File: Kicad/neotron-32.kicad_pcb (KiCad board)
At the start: 4 copper layers, 166.9 x 140.7 mm, 97 parts, among them J1001 Conn_02x05, J101 Conn_02x06, J102 Conn_02x06, J103 Conn_02x04, J201 DIN-5 180 degree, J202 DIN-5 180 degree, J301 3.5mm Audio Jack TRS, J302 Conn_01x03_Male, J401 USB_B, J501 micro SD Card, J601 Conn_02x13_Header, J701 AVR-ISP-6, J702 DE9 Male, J703 DE9 Male, J704 Double-mini-DIN-6, J901 DB15HD_Female, SW401 SW_Push_DPDT_ON_OFF, SW402 SW_Push_DPDT_ON_MO, U1001 ICL3232CPZMAX, U101 EK-TM4C123GXL, U201 74LS14, U202 6N138, U401 TC1262-33, U601 MCP23S17_SP, U701 ATmega328-PU, U801 MCP7940N-xP, Y801 32,768 Hz

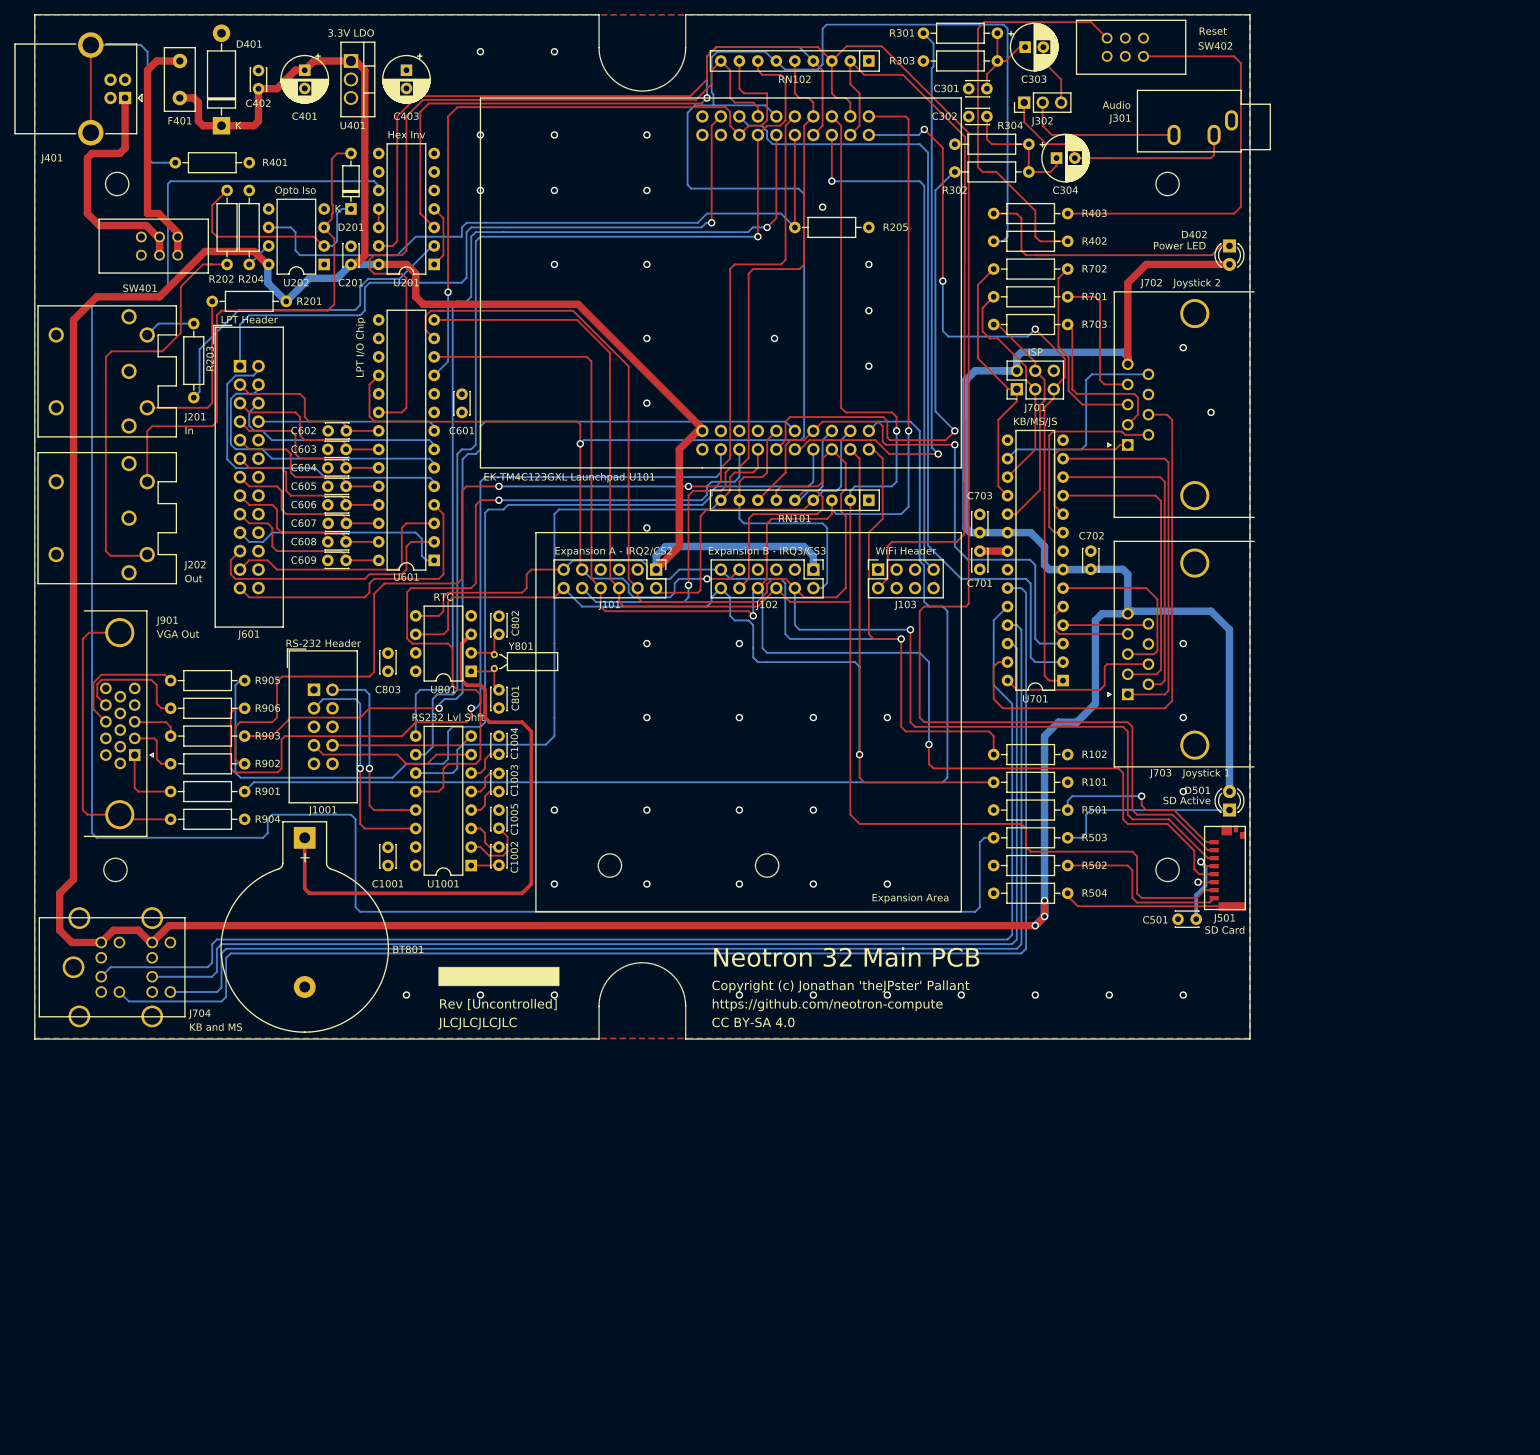
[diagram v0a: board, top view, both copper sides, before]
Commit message: Switch to 1598D enclosure.
Use MIC2005A current limiter on input.
Use soft on/off switch from Atmega.
Atmega connects to Tiva over I2C.
Use full-size SD card.
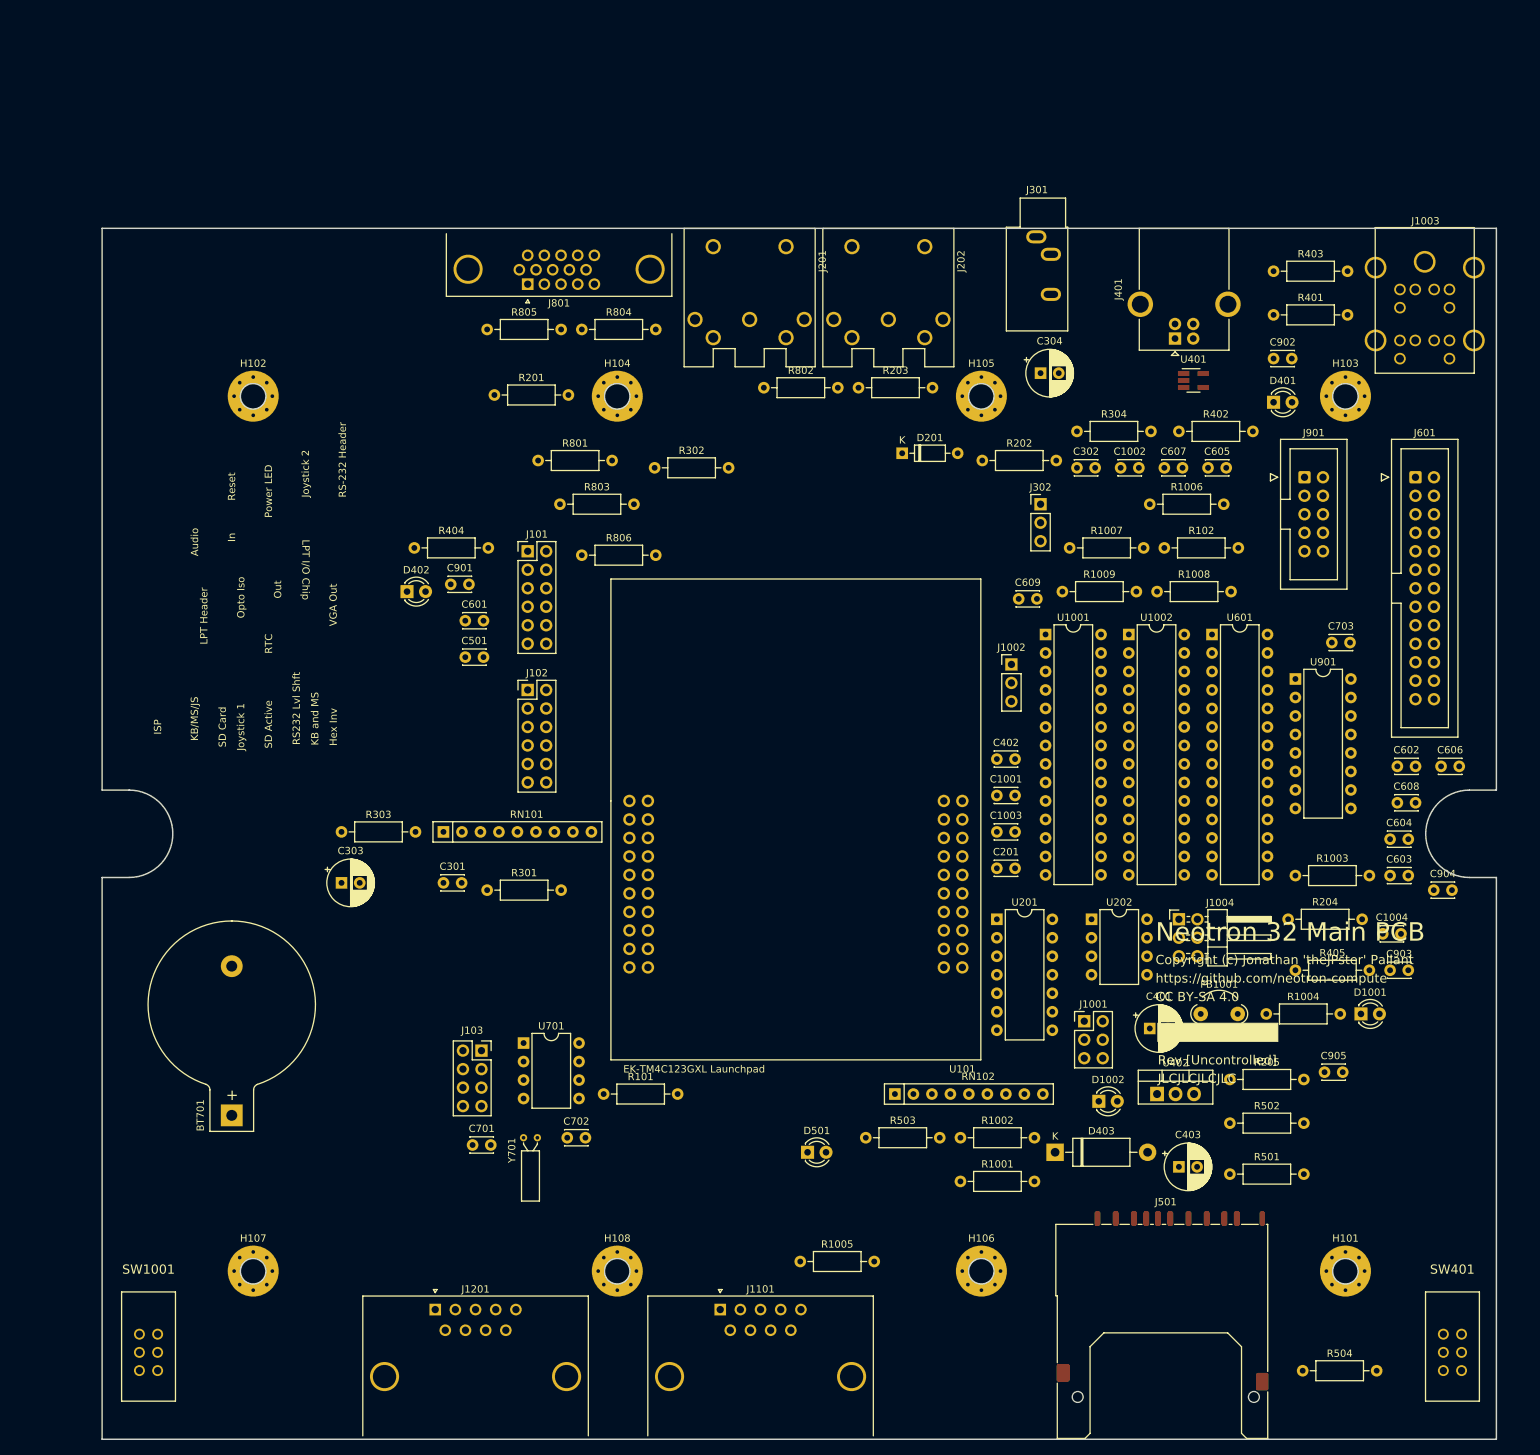
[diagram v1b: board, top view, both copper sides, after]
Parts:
- removed BT801: CR2032, Neotron 32:BatteryHolder_Keystone_103_1x20mm
- removed C1005, C803: 100n, Capacitor_THT:C_Disc_D3.0mm_W2.0mm_P2.50mm
- removed C801, C802: 6p, Capacitor_THT:C_Disc_D3.0mm_W2.0mm_P2.50mm
- removed F401: 250mA PTC, Fuse:Fuse_Littelfuse_395Series
- removed J701: AVR-ISP-6, Connector_PinHeader_2.54mm:PinHeader_2x03_P2.54mm_Vertical
- removed J702, J703: DE9 Male, Connector_Dsub:DSUB-9_Male_Horizontal_P2.77x2.84mm_EdgePinOffset14.56mm_Housed_MountingHolesOffset8.20mm
- removed J704: Double-mini-DIN-6, Neotron 32:Double_mini-DIN_6
- removed R701, R702, R703: 1k, Resistor_THT:R_Axial_DIN0207_L6.3mm_D2.5mm_P10.16mm_Horizontal
- removed R901, R902, R903, R905, R906: 330, Resistor_THT:R_Axial_DIN0207_L6.3mm_D2.5mm_P10.16mm_Horizontal
- removed R904: DNF, Resistor_THT:R_Axial_DIN0207_L6.3mm_D2.5mm_P10.16mm_Horizontal
- removed SW402: SW_Push_DPDT_ON_MO, Neotron 32:PHB2UEETS1A
- removed U801: MCP7940N-xP, Package_DIP:DIP-8_W7.62mm
- removed Y801: 32,768 Hz, Crystal:Crystal_C26-LF_D2.1mm_L6.5mm_Horizontal
- added BT701: CR2032, Neotron 32:BatteryHolder_Keystone_103_1x20mm, F.Cu at (97.9, 168.9)
- added C901: 100n, Capacitor_THT:C_Disc_D3.0mm_W2.0mm_P2.50mm, F.Cu at (128.0, 96.0)
- added C902: 100n, Capacitor_THT:C_Disc_D3.0mm_W2.0mm_P2.50mm, F.Cu at (241.0, 65.0)
- added C903: 100n, Capacitor_THT:C_Disc_D3.0mm_W2.0mm_P2.50mm, F.Cu at (257.0, 149.0)
- added C904: 100n, Capacitor_THT:C_Disc_D3.0mm_W2.0mm_P2.50mm, F.Cu at (263.0, 138.0)
- added C905: 100n, Capacitor_THT:C_Disc_D3.0mm_W2.0mm_P2.50mm, F.Cu at (248.0, 163.0)
- added D1001: LED, LED_THT:LED_D3.0mm, F.Cu at (253.0, 155.0)
- added D1002: LED, LED_THT:LED_D3.0mm, F.Cu at (217.0, 167.0)
- added D403: SA5.0A, Diode_THT:D_DO-15_P12.70mm_Horizontal, F.Cu at (211.0, 174.0)
- added FB1001: 100R, Ferrite_THT:LairdTech_28C0236-0JW-10, F.Cu at (231.0, 155.0)
- added H107: MountingHole, MountingHole:MountingHole_3.5mm_Pad_Via, F.Cu at (100.9, 190.3)
- added H108: MountingHole, MountingHole:MountingHole_3.5mm_Pad_Via, F.Cu at (150.9, 190.3)
- added J1002: 1x3 UART Debug Header, Connector_PinHeader_2.54mm:PinHeader_1x03_P2.54mm_Vertical, F.Cu at (205.0, 107.0)
- added J1003: Double-mini-DIN-6, Neotron 32:Double_mini-DIN_6, F.Cu at (261.8, 47.0)
- added J1004: AVR-ISP-6, Connector_PinHeader_2.54mm:PinHeader_2x03_P2.54mm_Horizontal, F.Cu at (228.0, 142.0)
- added J1101: DE9 Male, Connector_Dsub:DSUB-9_Male_Horizontal_P2.77x2.84mm_EdgePinOffset14.56mm_Housed_MountingHolesOffset8.20mm, F.Cu at (165.0, 195.6)
- added J1201: DE9 Male, Connector_Dsub:DSUB-9_Male_Horizontal_P2.77x2.84mm_EdgePinOffset14.56mm_Housed_MountingHolesOffset8.20mm, F.Cu at (125.9, 195.6)
- added J801: DB15HD_Female, Connector_Dsub:DSUB-15-HD_Female_Horizontal_P2.29x1.98mm_EdgePinOffset3.03mm_Housed_MountingHolesOffset4.94mm, F.Cu at (138.6, 54.8)
- added R1001: 10k, Resistor_THT:R_Axial_DIN0207_L6.3mm_D2.5mm_P10.16mm_Horizontal, F.Cu at (198.0, 178.0)
- added R1002: 10k, Resistor_THT:R_Axial_DIN0207_L6.3mm_D2.5mm_P10.16mm_Horizontal, F.Cu at (198.0, 172.0)
- added R1003: 10k, Resistor_THT:R_Axial_DIN0207_L6.3mm_D2.5mm_P10.16mm_Horizontal, F.Cu at (244.0, 136.0)
- added R1004: 1k, Resistor_THT:R_Axial_DIN0207_L6.3mm_D2.5mm_P10.16mm_Horizontal, F.Cu at (240.0, 155.0)
- added R1005: 1k, Resistor_THT:R_Axial_DIN0207_L6.3mm_D2.5mm_P10.16mm_Horizontal, F.Cu at (176.0, 189.0)
- added R1006: 6.81k 1%, Resistor_THT:R_Axial_DIN0207_L6.3mm_D2.5mm_P10.16mm_Horizontal, F.Cu at (224.0, 85.0)
- added R1007: 1k 1%, Resistor_THT:R_Axial_DIN0207_L6.3mm_D2.5mm_P10.16mm_Horizontal, F.Cu at (213.0, 91.0)
- added R1008: 6.81k 1%, Resistor_THT:R_Axial_DIN0207_L6.3mm_D2.5mm_P10.16mm_Horizontal, F.Cu at (225.0, 97.0)
- added R1009: 1k 1%, Resistor_THT:R_Axial_DIN0207_L6.3mm_D2.5mm_P10.16mm_Horizontal, F.Cu at (212.0, 97.0)
- added R404: 1k, Resistor_THT:R_Axial_DIN0207_L6.3mm_D2.5mm_P10.16mm_Horizontal, F.Cu at (123.0, 91.0)
- added R405: 330, Resistor_THT:R_Axial_DIN0207_L6.3mm_D2.5mm_P10.16mm_Horizontal, F.Cu at (244.0, 149.0)
- added R801: 330, Resistor_THT:R_Axial_DIN0207_L6.3mm_D2.5mm_P10.16mm_Horizontal, F.Cu at (140.0, 79.0)
- added R802: 330, Resistor_THT:R_Axial_DIN0207_L6.3mm_D2.5mm_P10.16mm_Horizontal, F.Cu at (171.0, 69.0)
- added R803: 330, Resistor_THT:R_Axial_DIN0207_L6.3mm_D2.5mm_P10.16mm_Horizontal, F.Cu at (143.0, 85.0)
- added R804: DNF, Resistor_THT:R_Axial_DIN0207_L6.3mm_D2.5mm_P10.16mm_Horizontal, F.Cu at (146.0, 61.0)
- added R805: 330, Resistor_THT:R_Axial_DIN0207_L6.3mm_D2.5mm_P10.16mm_Horizontal, F.Cu at (133.0, 61.0)
- added R806: 330, Resistor_THT:R_Axial_DIN0207_L6.3mm_D2.5mm_P10.16mm_Horizontal, F.Cu at (146.0, 92.0)
- added SW1001: SW_Push, Neotron 32:PHB2UEETS1A, F.Cu at (86.5, 200.7)
- added U1002: ATmega328P-PU, Package_DIP:DIP-28_W7.62mm, F.Cu at (221.1, 102.9)
- added U402: TC1262-33, Package_TO_SOT_THT:TO-220-3_Vertical, F.Cu at (225.0, 166.0)
- added U901: ICL3232CPZMAX, Package_DIP:DIP-16_W7.62mm, F.Cu at (244.0, 109.0)
- added Y701: 32,768 Hz, Crystal:Crystal_C26-LF_D2.1mm_L6.5mm_Horizontal, F.Cu at (138.0, 172.0)
- C701, C702: value 100n -> 6p
- D401: value SA5.0A -> LED; footprint Diode_THT:D_DO-15_P12.70mm_Horizontal -> LED_THT:LED_D3.0mm
- D402: value Red LED -> LED
- H101, H102, H103, H104, H105, H106: footprint MountingHole:MountingHole_3.2mm_M3 -> MountingHole:MountingHole_3.5mm_Pad_Via
- J1001: value Conn_02x05 -> 2x3 Header; footprint Connector_IDC:IDC-Header_2x05_P2.54mm_Vertical -> Connector_PinHeader_2.54mm:PinHeader_2x03_P2.54mm_Vertical
- J501: value micro SD Card -> SD_Card; footprint Neotron 32:Molex_4730_2651 -> Connector_Card:SD_Kyocera_145638109511859+
- J901: value DB15HD_Female -> Conn_02x05; footprint Connector_Dsub:DSUB-15-HD_Female_Horizontal_P2.29x1.98mm_EdgePinOffset3.03mm_Housed_MountingHolesOffset4.94mm -> Connector_IDC:IDC-Header_2x05_P2.54mm_Vertical
- R402: value 330 -> 100k
- R403: value 330 -> 1k
- SW401: value SW_Push_DPDT_ON_OFF -> SW_Push_DPDT_ON_MO
- U1001: value ICL3232CPZMAX -> MCP23017_SP; footprint Package_DIP:DIP-16_W7.62mm -> Package_DIP:DIP-28_W7.62mm
- U401: value TC1262-33 -> MIC2005A-2YM5; footprint Package_TO_SOT_THT:TO-220-3_Vertical -> Package_TO_SOT_SMD:SOT-23-5_HandSoldering
- U701: value ATmega328-PU -> MCP7940N-xP; footprint Package_DIP:DIP-28_W7.62mm -> Package_DIP:DIP-8_W7.62mm
- moved SW401 233.8 mm to (265.6, 200.7), turned to 270 degrees
- moved C403 184.2 mm to (228.0, 176.0), turned to 0 degrees
- moved H103 181.0 mm to (250.9, 70.2)
- moved C401 175.5 mm to (224.0, 157.0), turned to 0 degrees
- moved R204 174.3 mm to (243.0, 142.0), turned to 0 degrees
- moved J901 165.1 mm to (245.2, 81.3), turned to 0 degrees
- moved J601 162.1 mm to (260.5, 81.3)
- moved C603 157.2 mm to (257.0, 136.0)
- moved C606 157.0 mm to (264.0, 121.0)
- moved C604 154.5 mm to (257.0, 131.0)
- moved C602 153.9 mm to (258.0, 121.0)
- moved C608 151.2 mm to (258.0, 126.0)
- moved D401 149.4 mm to (241.0, 71.0), turned to 0 degrees
- moved C303 148.3 mm to (113.0, 137.0)
- moved J401 147.9 mm to (227.5, 62.2), turned to 90 degrees
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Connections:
- net /Power/UNFUSED_5V renamed Net-(R405-Pad2)
- C1001 pad 1: GND -> +5V
- C1001 pad 2: +3V3 -> GND
- C1002 pad 1: Net-(C1002-Pad1) -> GND
- C1003 pad 1: Net-(C1003-Pad1) -> +5V
- C1003 pad 2: Net-(C1003-Pad2) -> GND
- C1004 pad 1: GND -> Net-(C1004-Pad1)
- C1004 pad 2: Net-(C1004-Pad2) -> GND
- C702 pad 1: +5V -> Net-(C702-Pad1)
- C703 pad 1: +5V -> +3V3
- D401 pad 1: +5V -> Net-(D401-Pad1)
- D401 pad 2: GND -> Net-(D401-Pad2)
- D402 pad 1: Net-(D402-Pad1) -> GND
- D402 pad 2: +5V -> Net-(D402-Pad2)
- J1001 pad 1: Net-(J1001-Pad1) -> +5V
- J1001 pad 2: /RS-232 Serial Port/RS232_RX_IN -> Net-(J1001-Pad2)
- J1001 pad 3: /RS-232 Serial Port/RS232_TX_OUT -> +5V
- J1001 pad 5: GND -> +5V
- J103 pad 3: Net-(J103-Pad3) -> (no net)
- J103 pad 4: Net-(J103-Pad4) -> (no net)
- J103 pad 5: Net-(J103-Pad5) -> (no net)
- J103 pad 6: Net-(J103-Pad6) -> (no net)
- J201 pad 1: Net-(J201-Pad1) -> (no net)
- J201 pad 3: Net-(J201-Pad3) -> (no net)
- J202 pad 1: Net-(J202-Pad1) -> (no net)
- J202 pad 2: Net-(J202-Pad2) -> (no net)
- J202 pad 3: Net-(J202-Pad3) -> (no net)
- J401 pad 1: /Power/VUSB -> Net-(D401-Pad2)
- J401 pad 2: Net-(J401-Pad2) -> (no net)
- J401 pad 3: Net-(J401-Pad3) -> (no net)
- J501 pad 1: Net-(J501-Pad1) -> /~PA3_SPI_CS0
- J501 pad 12: (no net) -> Net-(J501-Pad12)
- J501 pad 2: /~PA3_SPI_CS0 -> /PA5_SPI_MOSI
- J501 pad 3: /PA5_SPI_MOSI -> GND
- J901 pad 1: Net-(J901-Pad1) -> (no net)
- J901 pad 10: Net-(J901-Pad10) -> (no net)
- J901 pad 2: Net-(J901-Pad2) -> /RS-232 Serial Port/RS232_RX_IN
- J901 pad 3: Net-(J901-Pad3) -> /RS-232 Serial Port/RS232_TX_OUT
- J901 pad 4: Net-(J901-Pad4) -> (no net)
- J901 pad 6: GND -> (no net)
- J901 pad 7: GND -> /RS-232 Serial Port/RS232_RTS_OUT
- J901 pad 8: GND -> /RS-232 Serial Port/RS232_CTS_IN
- J901 pad 9: Net-(J901-Pad9) -> (no net)
- R402 pad 1: /~RESET -> /~POWER_ON
- R402 pad 2: Net-(R402-Pad2) -> Net-(D401-Pad2)
- R403 pad 1: Net-(D402-Pad1) -> Net-(R403-Pad1)
- R403 pad 2: Net-(R403-Pad2) -> Net-(D401-Pad1)
- R501 pad 1: Net-(J501-Pad1) -> Net-(J501-Pad9)
- R504 pad 1: Net-(J501-Pad9) -> Net-(J501-Pad12)
- RN101 pad 7: /PE1_U7TX -> (no net)
- SW401 pad 1: Net-(SW401-Pad1) -> (no net)
- SW401 pad 2: /Power/VUSB -> GND
- SW401 pad 4: Net-(SW401-Pad4) -> (no net)
- SW401 pad 5: /Power/VUSB -> GND
- U1001 pad 1: Net-(C1002-Pad2) -> /Keyboard, Mouse and Joystick/JS1_UP
- U1001 pad 10: /PC4_U1RTS -> GND
- U1001 pad 11: /PB1_U1TX -> (no net)
- U1001 pad 12: /PB0_U1RX -> /PA6_I2C_SCL
- U1001 pad 13: /RS-232 Serial Port/RS232_RX_IN -> /PA7_I2C_SDA
- U1001 pad 14: /RS-232 Serial Port/RS232_TX_OUT -> (no net)
- U1001 pad 15: GND -> Net-(J1001-Pad6)
- U1001 pad 16: +3V3 -> Net-(J1001-Pad4)
- U1001 pad 2: Net-(C1005-Pad2) -> /Keyboard, Mouse and Joystick/JS1_DOWN
- U1001 pad 3: Net-(C1002-Pad1) -> /Keyboard, Mouse and Joystick/JS1_LEFT
- U1001 pad 4: Net-(C1003-Pad1) -> /Keyboard, Mouse and Joystick/JS1_RIGHT
- U1001 pad 5: Net-(C1003-Pad2) -> /Keyboard, Mouse and Joystick/JS1_A_B
- U1001 pad 6: Net-(C1004-Pad2) -> /Keyboard, Mouse and Joystick/JS1_START_C
- U1001 pad 7: /RS-232 Serial Port/RS232_RTS_OUT -> /Keyboard, Mouse and Joystick/JS1_SELECT
- U1001 pad 8: /RS-232 Serial Port/RS232_CTS_IN -> (no net)
- U1001 pad 9: /PC5_U1CTS -> +5V
- U101 pad 1.1: +3.3VP -> (no net)
- U101 pad 2.3: /PE0_U7RX -> (no net)
- U101 pad 3.3: Net-(U101-Pad3.3) -> (no net)
- U101 pad 3.4: Net-(U101-Pad3.4) -> (no net)
- U101 pad 3.7: /PE1_U7TX -> (no net)
- U101 pad 4.1: Net-(U101-Pad4.1) -> (no net)
- U101 pad 4.10: /~PF4_AT_RESET -> /~PF4_HID_IRQ
- U101 pad 4.2: Net-(U101-Pad4.2) -> (no net)
- U201 pad 6: Net-(U201-Pad6) -> (no net)
- U201 pad 8: Net-(U201-Pad8) -> (no net)
- U202 pad 1: Net-(U202-Pad1) -> (no net)
- U202 pad 4: Net-(U202-Pad4) -> (no net)
- U401 pad 1: +5V -> Net-(D401-Pad2)
- U401 pad 3: +3V3 -> /~POWER_ON
- U601 pad 19: Net-(U601-Pad19) -> (no net)
- U701 pad 1: /~PF4_AT_RESET -> Net-(C701-Pad2)
- U701 pad 2: /PE0_U7RX -> Net-(C702-Pad1)
- U701 pad 3: /PE1_U7TX -> +BATT
- U701 pad 4: /Keyboard, Mouse and Joystick/START_C_JS1 -> GND
- U701 pad 5: /Keyboard, Mouse and Joystick/RIGHT_GND_JS1 -> /PA7_I2C_SDA
- U701 pad 6: /Keyboard, Mouse and Joystick/LEFT_GND_JS1 -> /PA6_I2C_SCL
- U701 pad 7: +5V -> (no net)
- U701 pad 8: GND -> +3V3
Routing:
- net +5V: track 644.0 -> 0.00 mm, vias 3 -> 0
- net Net-(R503-Pad2): track 277.2 -> 0.00 mm
- net /~RESET: track 270.9 -> 0.00 mm, vias 2 -> 0
- net /PA2_SPI_CLK: track 270.8 -> 0.00 mm, vias 3 -> 0
- net /PA4_SPI_MISO: track 263.1 -> 0.00 mm, vias 1 -> 0
- net /~PA3_SPI_CS0: track 261.3 -> 0.00 mm
- net /PA5_SPI_MOSI: track 223.7 -> 0.00 mm, vias 1 -> 0
- net /Keyboard, Mouse and Joystick/KB_CLK: track 182.9 -> 0.00 mm
- net /Keyboard, Mouse and Joystick/KB_DAT: track 175.9 -> 0.00 mm
- net /Keyboard, Mouse and Joystick/MS_CLK: track 167.7 -> 0.00 mm
- net /Keyboard, Mouse and Joystick/MS_DAT: track 163.6 -> 0.00 mm
- net /PB7_VGA_GREEN: track 160.9 -> 0.00 mm, vias 2 -> 0
- net /PF1_VGA_RED: track 155.7 -> 0.00 mm
- net /PA6_I2C_SCL: track 153.2 -> 0.00 mm, vias 1 -> 0
- net /PC4_U1RTS: track 145.5 -> 0.00 mm, vias 1 -> 0
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- removed copper zone on Vcc.Cu, net +3V3
- removed copper zone on B.Cu, net GND
- removed copper zone on F.Cu, net GND
- removed copper zone on Gnd.Cu, net GND
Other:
- board size 166.9 x 140.7 mm -> 191.5 x 166.3 mm
- board text added: "12.00"
- board text added: "120.15"
- board text added: "166.30"
- board text added: "191.48"
- board text added: "20.74"
- board text added: "23.07"
- board text added: "50.00"
- board text added: "77.15"
- board text added: "9.71"
- board text added: "[.38]"
- board text added: "[.47]"
- board text added: "[.82]"
- board text added: "[.91]"
- board text added: "[1.97]"
- board text added: "[3.04]"
- board text added: "[4.73]"
- board text added: "[6.55]"
- board text added: "[7.54]"
- board text added: "∅3.51 [∅0.14]"
- board text removed: "3.3V LDO"
- board text removed: "Expansion A - IRQ2/CS2"
- board text removed: "Expansion Area"
- board text removed: "Expansion B - IRQ3/CS3"
- board text removed: "WiFi Header"

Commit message: Working on layout.
Laid out the parallel port - reordered some pins to make it easier.
Set the minimum track widths to 6 mil/6 mil with a 6mm/3mm via.
Replaced the SPST power switch with a PUE to match the reset switch.
Attached some existing 3D models to the PCB footprints.
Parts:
- added R1010: 10k, Resistor_THT:R_Axial_DIN0207_L6.3mm_D2.5mm_P10.16mm_Horizontal, F.Cu at (85.2, 176.5)
- J1004: footprint Connector_PinHeader_2.54mm:PinHeader_2x03_P2.54mm_Horizontal -> Connector_PinHeader_2.54mm:PinHeader_2x03_P2.54mm_Vertical
- SW1001: value SW_Push -> SW_Push_DPDT_ON_MO
- moved U402 117.7 mm to (249.1, 50.8), turned to 180 degrees
- moved C601 106.9 mm to (227.5, 144.8), turned to 270 degrees
- moved J601 87.1 mm to (216.0, 156.2), turned to 180 degrees
- moved C902 85.6 mm to (259.2, 148.6)
- moved U1001 84.7 mm to (167.8, 176.5), turned to 270 degrees
- moved R301 84.7 mm to (200.2, 86.4), turned to 90 degrees
- moved C401 83.0 mm to (207.8, 75.6)
- moved C605 65.2 mm to (224.9, 144.8), turned to 180 degrees
- moved C703 65.2 mm to (263.0, 167.7), turned to 270 degrees
- moved C1001 62.9 mm to (257.0, 92.6)
- moved C1003 62.9 mm to (257.0, 97.6)
- moved J1004 62.0 mm to (265.6, 92.7)
- moved J901 60.4 mm to (257.9, 140.4), turned to 270 degrees
- moved C607 57.2 mm to (224.9, 137.2), turned to 180 degrees
- moved U201 56.8 mm to (217.3, 87.0)
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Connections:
- SW1001 pad 1: /~POWER_ON -> (no net)
- SW1001 pad 3: (no net) -> Net-(R1010-Pad2)
- SW1001 pad 5: (no net) -> GND
- SW1001 pad 6: (no net) -> Net-(R1010-Pad2)
- U1002 pad 13: /~POWER_ON -> Net-(R1010-Pad2)
- U601 pad 1: /Parallel Printer/ACK -> /Parallel Printer/SELECT
- U601 pad 2: /Parallel Printer/~BUSY -> /Parallel Printer/POUT
- U601 pad 3: /Parallel Printer/POUT -> /Parallel Printer/~BUSY
- U601 pad 4: /Parallel Printer/SELECT -> /Parallel Printer/ACK
- U601 pad 5: /Parallel Printer/~LF -> /Parallel Printer/~SELPRI
- U601 pad 6: /Parallel Printer/ERROR -> /Parallel Printer/RESET
- U601 pad 7: /Parallel Printer/RESET -> /Parallel Printer/ERROR
- U601 pad 8: /Parallel Printer/~SELPRI -> /Parallel Printer/~LF
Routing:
- net /Parallel Printer/~LF: track 0.00 -> 55.7 mm
- net /Parallel Printer/RESET: track 0.00 -> 54.5 mm, vias 0 -> 1
- net /Parallel Printer/D0: track 0.00 -> 29.3 mm
- net /Parallel Printer/~SELPRI: track 0.00 -> 29.1 mm
- net /Parallel Printer/D1: track 0.00 -> 28.4 mm
- net /Parallel Printer/D2: track 0.00 -> 27.6 mm
- net /Parallel Printer/D6: track 0.00 -> 27.3 mm
- net /Parallel Printer/D5: track 0.00 -> 26.3 mm
- net /Parallel Printer/D4: track 0.00 -> 26.3 mm
- net /Parallel Printer/D3: track 0.00 -> 26.3 mm
- net /Parallel Printer/ERROR: track 0.00 -> 25.1 mm
- net /Parallel Printer/D7: track 0.00 -> 19.3 mm
- net /Parallel Printer/~BUSY: track 0.00 -> 16.1 mm
- net /Parallel Printer/ACK: track 0.00 -> 15.5 mm
- net /Parallel Printer/SELECT: track 0.00 -> 14.5 mm
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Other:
- copper layers 4 -> 2
- net class Default: clearance 0.254 -> 0.1524; trace_width 0.254 -> 0.1524; via_dia 1.016 -> 0.635; via_drill 0.635 -> 0.3
- net class Power: trace_width 0.508 -> 0.254; via_dia 1.016 -> 0.635; via_drill 0.635 -> 0.3
- rule trace_clearance: 0.254 -> 0.1524
- rule trace_min: 0.2032 -> 0.1524
- rule via_min_drill: 0.3048 -> 0.3
- rule via_min_size: 0.4064 -> 0.6
